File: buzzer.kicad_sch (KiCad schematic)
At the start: 0 parts

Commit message: Buzzer sheet 1st draft finished
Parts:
- added J1: Conn_01x02, symbol Connector_Generic:Conn_01x02
- added R5, R6: R, symbol Hestres_Standard_Lib:R
- added U4: UCC23313DWYR, SOIC6_DWY_TEX, symbol ProjGateDriver:UCC23313DWYR
- added U5: RD3L01BATTL1, DPAK_1BATTL1_ROM, symbol ProjPMOS:RD3L01BATTL1
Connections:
- new net: R6.1, U4.5 (VOUT)
- new net: J1.1 (Pin_1), R5.1, U5.2 (Drain)
- new net: R6.2, U5.1 (Gate)
- new net 18V: U4.6 (VCC), U5.3 (Source)
- new net GND: J1.2 (Pin_2), R5.2, U4.3 (CATHODE), U4.4 (VEE)
- new net PWM: U4.1 (ANODE)
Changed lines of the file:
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@@
 (kicad_sch (version 20230121) (generator eeschema)
   (paper "A4")
+  (junction (at 181.61 87.63) (diameter 0) (color 0 0 0 0)
+  )
+  (junction (at 69.85 132.715) (diameter 0) (color 0 0 0 0)
+  )
+  (junction (at 115.57 132.715) (diameter 0) (color 0 0 0 0)
+  )
+  (junction (at 182.88 125.095) (diameter 0) (color 0 0 0 0)
+  )
+  (junction (at 182.88 132.715) (diameter 0) (color 0 0 0 0)
+  )
+  (wire (pts (xy 193.675 125.095) (xy 182.88 125.095))
+    (stroke (width 0) (type default))
+  )
+  (wire (pts (xy 182.88 109.855) (xy 182.88 125.095))
+    (stroke (width 0) (type default))
+  )
+  (wire (pts (xy 115.57 107.315) (xy 121.92 107.315))
+    (stroke (width 0) (type default))
+  )
+  (wire (pts (xy 193.675 132.715) (xy 182.88 132.715))
+    (stroke (width 0) (type default))
+  )
+  (wire (pts (xy 69.85 132.715) (xy 115.57 132.715))
+    (stroke (width 0) (type default))
+  )
+  (wire (pts (xy 115.57 132.715) (xy 182.88 132.715))
+    (stroke (width 0) (type default))
+  )
+  (wire (pts (xy 180.975 109.855) (xy 182.88 109.855))
+    (stroke (width 0) (type default))
+  )
+  (wire (pts (xy 129.54 107.315) (xy 135.255 107.315))
+    (stroke (width 0) (type default))
+  )
+  (wire (pts (xy 115.57 87.63) (xy 181.61 87.63))
+    (stroke (width 0) (type default))
+  )
+  (wire (pts (xy 67.31 132.715) (xy 69.85 132.715))
+    (stroke (width 0) (type default))
+  )
+  (wire (pts (xy 193.675 130.175) (xy 193.675 132.715))
+    (stroke (width 0) (type default))
+  )
+  (wire (pts (xy 193.675 127.635) (xy 193.675 125.095))
+    (stroke (width 0) (type default))
+  )
+  (wire (pts (xy 67.31 104.775) (xy 69.85 104.775))
+    (stroke (width 0) (type default))
+  )
+  (wire (pts (xy 115.57 109.855) (xy 115.57 132.715))
+    (stroke (width 0) (type default))
+  )
+  (wire (pts (xy 69.85 109.855) (xy 69.85 132.715))
+    (stroke (width 0) (type default))
+  )
+  (wire (pts (xy 180.975 107.315) (xy 181.61 107.315))
+    (stroke (width 0) (type default))
+  )
+  (wire (pts (xy 181.61 107.315) (xy 181.61 87.63))
+    (stroke (width 0) (type default))
+  )
+  (wire (pts (xy 115.57 87.63) (xy 115.57 104.775))
+    (stroke (width 0) (type default))
+  )
+  (wire (pts (xy 181.61 87.63) (xy 183.515 87.63))
+    (stroke (width 0) (type default))
+  )
+  (hierarchical_label "GND" (shape input) (at 67.31 132.715 180) (fields_autoplaced)
+    (effects (font (size 1.27 1.27)) (justify right))
+  )
+  (hierarchical_label "PWM" (shape input) (at 67.31 104.775 180) (fields_autoplaced)
+    (effects (font (size 1.27 1.27)) (justify right))
+  )
+  (hierarchical_label "18V" (shape input) (at 183.515 87.63 0) (fields_autoplaced)
+    (effects (font (size 1.27 1.27)) (justify left))
+  )
+  (symbol (lib_id "ProjGateDriver:UCC23313DWYR") (at 69.85 104.775 0) (unit 1)
+    (in_bom yes) (on_board yes) (dnp no) (fields_autoplaced)
+    (property "Reference" "U4" (at 92.71 94.615 0)
+      (effects (font (size 1.524 1.524)))
+    )
+    (property "Value" "UCC23313DWYR" (at 92.71 97.155 0)
+      (effects (font (size 1.524 1.524)))
+    )
+    (property "Footprint" "SOIC6_DWY_TEX" (at 69.85 104.775 0)
+      (effects (font (size 1.27 1.27) italic) hide)
+    )
+    (property "Datasheet" "UCC23313DWYR" (at 69.85 104.775 0)
+      (effects (font (size 1.27 1.27) italic) hide)
+    )
+    (pin "1")
+    (pin "2")
+    (pin "3")
+    (pin "4")
+    (pin "5")
+    (pin "6")
+    (instances
+      (project "CatLasers"
+        (path "/b94f5b10-ee0c-4425-b025-e3a8bb3cc7b0/d2efd2c4-3cc3-446b-9153-cc0ad0bf95db"
+          (reference "U4") (unit 1)
+        )
+      )
+    )
+  )
+  (symbol (lib_id "Hestres_Standard_Lib:R") (at 182.88 128.905 0) (unit 1)
+    (in_bom yes) (on_board yes) (dnp no) (fields_autoplaced)
+    (property "Reference" "R5" (at 184.785 127.635 0)
+      (effects (font (size 1.27 1.27)) (justify left))
+    )
+    (property "Value" "R" (at 184.785 130.175 0)
+      (effects (font (size 1.27 1.27)) (justify left))
+    )
+    (property "Footprint" "" (at 181.102 128.905 90)
+      (effects (font (size 1.27 1.27)) hide)
+    )
+    (property "Datasheet" "~" (at 182.88 128.905 0)
+      (effects (font (size 1.27 1.27)) hide)
+    )
+    (pin "1")
+    (pin "2")
+    (instances
+      (project "CatLasers"
+        (path "/b94f5b10-ee0c-4425-b025-e3a8bb3cc7b0/d2efd2c4-3cc3-446b-9153-cc0ad0bf95db"
+          (reference "R5") (unit 1)
+        )
+      )
+    )
+  )
+  (symbol (lib_id "Connector_Generic:Conn_01x02") (at 198.755 127.635 0) (unit 1)
+    (in_bom yes) (on_board yes) (dnp no) (fields_autoplaced)
+    (property "Reference" "J1" (at 201.93 127.635 0)
+      (effects (font (size 1.27 1.27)) (justify left))
+    )
+    (property "Value" "Conn_01x02" (at 201.93 130.175 0)
+      (effects (font (size 1.27 1.27)) (justify left))
+    )
+    (property "Footprint" "" (at 198.755 127.635 0)
+      (effects (font (size 1.27 1.27)) hide)
+    )
+    (property "Datasheet" "~" (at 198.755 127.635 0)
+      (effects (font (size 1.27 1.27)) hide)
+    )
+    (pin "1")
+    (pin "2")
+    (instances
+      (project "CatLasers"
+        (path "/b94f5b10-ee0c-4425-b025-e3a8bb3cc7b0/d2efd2c4-3cc3-446b-9153-cc0ad0bf95db"
+          (reference "J1") (unit 1)
+        )
+      )
+    )
+  )
+  (symbol (lib_id "ProjPMOS:RD3L01BATTL1") (at 135.255 107.315 0) (unit 1)
+    (in_bom yes) (on_board yes) (dnp no) (fields_autoplaced)
+    (property "Reference" "U5" (at 158.115 97.155 0)
+      (effects (font (size 1.524 1.524)))
+    )
+    (property "Value" "RD3L01BATTL1" (at 158.115 99.695 0)
+      (effects (font (size 1.524 1.524)))
+    )
+    (property "Footprint" "DPAK_1BATTL1_ROM" (at 135.255 107.315 0)
+      (effects (font (size 1.27 1.27) italic) hide)
+    )
+    (property "Datasheet" "RD3L01BATTL1" (at 135.255 107.315 0)
+      (effects (font (size 1.27 1.27) italic) hide)
+    )
+    (pin "1")
+    (pin "2")
+    (pin "3")
+    (instances
+      (project "CatLasers"
+        (path "/b94f5b10-ee0c-4425-b025-e3a8bb3cc7b0/d2efd2c4-3cc3-446b-9153-cc0ad0bf95db"
+          (reference "U5") (unit 1)
+        )
+      )
+    )
+  )
+  (symbol (lib_id "Hestres_Standard_Lib:R") (at 125.73 107.315 90) (unit 1)
+    (in_bom yes) (on_board yes) (dnp no) (fields_autoplaced)
+    (property "Reference" "R6" (at 125.73 101.6 90)
+      (effects (font (size 1.27 1.27)))
+    )
+    (property "Value" "R" (at 125.73 104.14 90)
+      (effects (font (size 1.27 1.27)))
+    )
+    (property "Footprint" "" (at 125.73 109.093 90)
+      (effects (font (size 1.27 1.27)) hide)
+    )
+    (property "Datasheet" "~" (at 125.73 107.315 0)
+      (effects (font (size 1.27 1.27)) hide)
+    )
+    (pin "1")
+    (pin "2")
+    (instances
+      (project "CatLasers"
+        (path "/b94f5b10-ee0c-4425-b025-e3a8bb3cc7b0/d2efd2c4-3cc3-446b-9153-cc0ad0bf95db"
+          (reference "R6") (unit 1)
+        )
+      )
+    )
+  )
 )

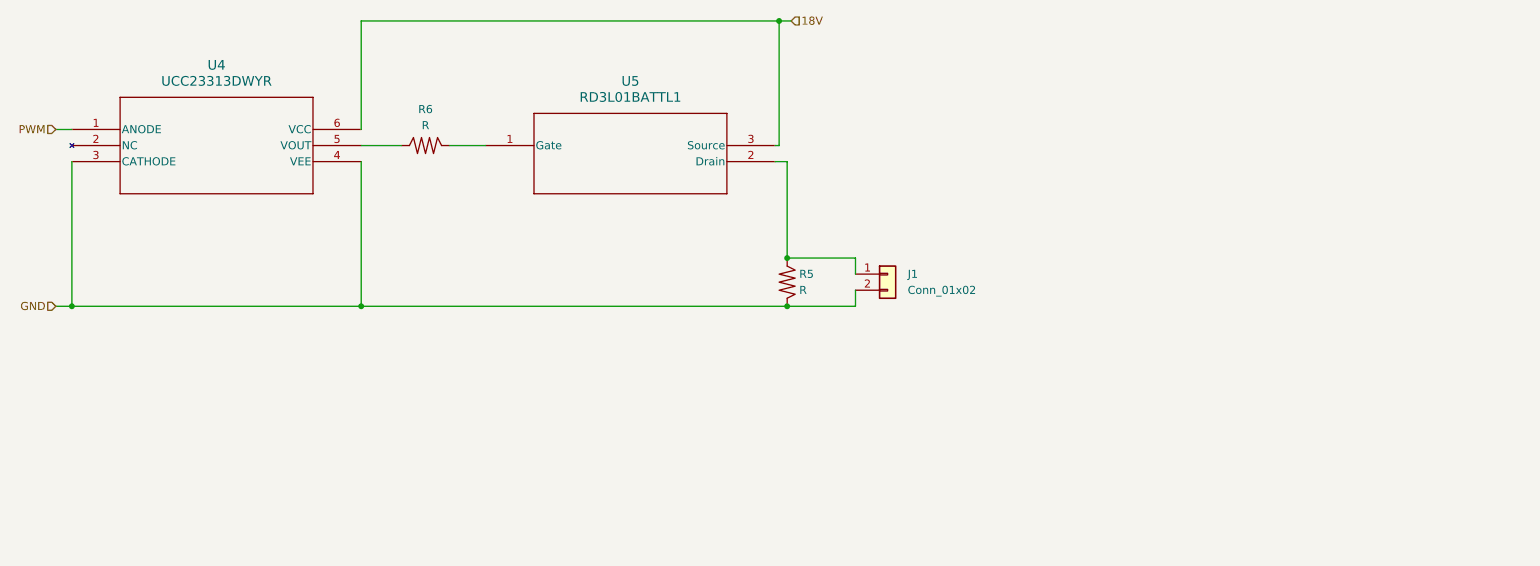
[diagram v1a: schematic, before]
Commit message: Gate Driver resistor chosen and footprint added
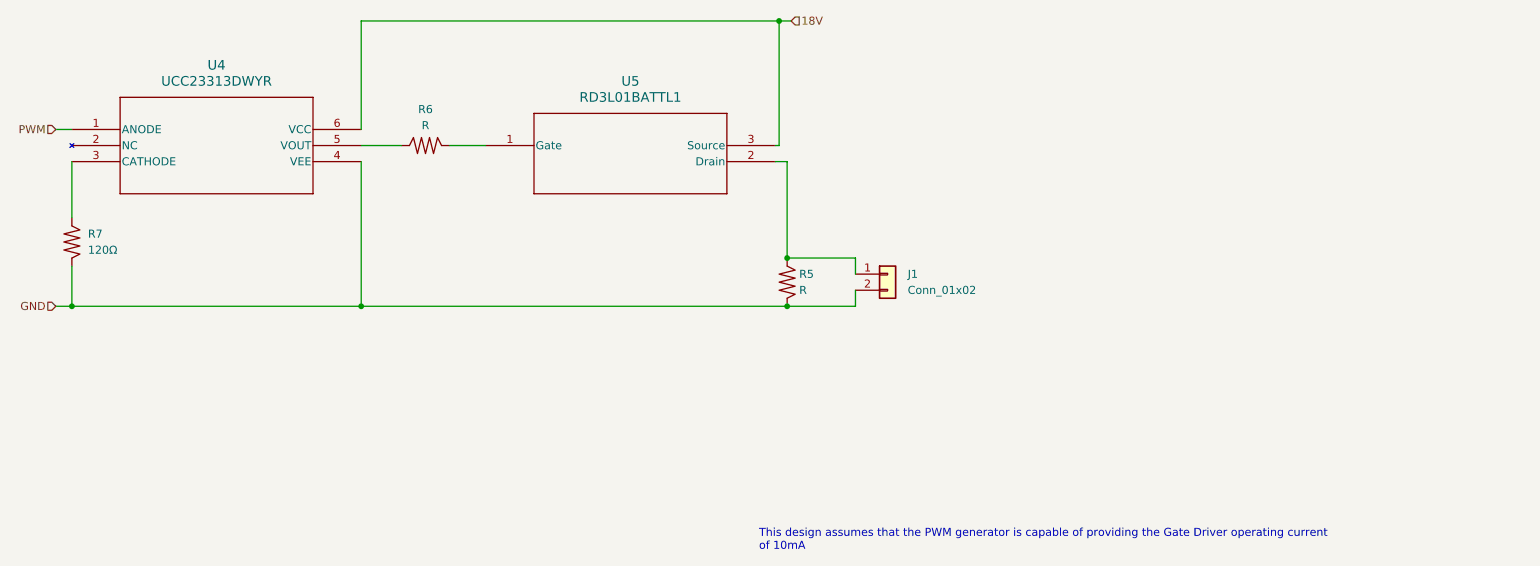
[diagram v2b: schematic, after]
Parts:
- added R7: 120Ω, Resistor_SMD:R_0805_2012Metric, symbol Hestres_Standard_Lib:R
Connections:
- net GND: now also R7.2; no longer U4.3 (CATHODE)
- new net: R7.1, U4.3 (CATHODE)
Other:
- note added: "This design assumes that the PWM generator is capable of providing the Gate Driver operating current of 10mA"
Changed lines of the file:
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@@
+    (stroke (width 0) (type default))
+  )
+  (wire (pts (xy 69.85 126.365) (xy 69.85 132.715))
     (stroke (width 0) (type default))
   )
@@
     (stroke (width 0) (type default))
   )
-  (wire (pts (xy 69.85 109.855) (xy 69.85 132.715))
+  (wire (pts (xy 69.85 109.855) (xy 69.85 118.745))
     (stroke (width 0) (type default))
   )
@@
   (wire (pts (xy 181.61 87.63) (xy 183.515 87.63))
     (stroke (width 0) (type default))
+  )
+  (text "This design assumes that the PWM generator is capable of providing the Gate Driver operating current \nof 10mA"
+    (at 178.435 171.45 0)
+    (effects (font (size 1.27 1.27)) (justify left bottom))
   )
   (hierarchical_label "GND" (shape input) (at 67.31 132.715 180) (fields_autoplaced)
@@
         )
       )
+    )
+  )
+  (symbol (lib_id "Hestres_Standard_Lib:R") (at 69.85 122.555 0) (unit 1)
+    (in_bom yes) (on_board yes) (dnp no) (fields_autoplaced)
+    (property "Reference" "R7" (at 72.39 121.285 0)
+      (effects (font (size 1.27 1.27)) (justify left))
+    )
+    (property "Value" "120Ω" (at 72.39 123.825 0)
+      (effects (font (size 1.27 1.27)) (justify left))
+    )
+    (property "Footprint" "Resistor_SMD:R_0805_2012Metric" (at 68.072 122.555 90)
+      (effects (font (size 1.27 1.27)) hide)
+    )
+    (property "Datasheet" "~" (at 69.85 122.555 0)
+      (effects (font (size 1.27 1.27)) hide)
+    )
+    (pin "1")
+    (pin "2")
+    (instances
+      (project "CatLasers"
+        (path "/b94f5b10-ee0c-4425-b025-e3a8bb3cc7b0/d2efd2c4-3cc3-446b-9153-cc0ad0bf95db"
+          (reference "R7") (unit 1)
+        )
+      )

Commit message: Some cleanup
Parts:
- U4: footprint SOIC6_DWY_TEX -> (none)
- U5: footprint DPAK_1BATTL1_ROM -> (none)
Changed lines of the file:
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@@
       (effects (font (size 1.524 1.524)))
     )
-    (property "Footprint" "SOIC6_DWY_TEX" (at 69.85 104.775 0)
+    (property "Footprint" "" (at 69.85 104.775 0)
       (effects (font (size 1.27 1.27) italic) hide)
     )
@@
       (effects (font (size 1.524 1.524)))
     )
-    (property "Footprint" "DPAK_1BATTL1_ROM" (at 135.255 107.315 0)
+    (property "Footprint" "" (at 135.255 107.315 0)
       (effects (font (size 1.27 1.27) italic) hide)
     )

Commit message: Remaining Footprints Assigned
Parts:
- J1: footprint (none) -> Connector_PinHeader_2.54mm:PinHeader_1x02_P2.54mm_Vertical
- R5, R6: footprint (none) -> Resistor_SMD:R_0805_2012Metric
- U4: footprint (none) -> Proj:SOD-123FL_MCC
- U5: footprint (none) -> Proj:RD3L01BATTL1_ROM
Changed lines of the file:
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@@
       (effects (font (size 1.524 1.524)))
     )
-    (property "Footprint" "" (at 69.85 104.775 0)
+    (property "Footprint" "Proj:SOD-123FL_MCC" (at 69.85 104.775 0)
       (effects (font (size 1.27 1.27) italic) hide)
     )
@@
       (effects (font (size 1.27 1.27)) (justify left))
     )
-    (property "Footprint" "" (at 181.102 128.905 90)
+    (property "Footprint" "Resistor_SMD:R_0805_2012Metric" (at 181.102 128.905 90)
       (effects (font (size 1.27 1.27)) hide)
     )
@@
       (effects (font (size 1.27 1.27)) (justify left))
     )
-    (property "Footprint" "" (at 198.755 127.635 0)
+    (property "Footprint" "Connector_PinHeader_2.54mm:PinHeader_1x02_P2.54mm_Vertical" (at 198.755 127.635 0)
       (effects (font (size 1.27 1.27)) hide)
     )
@@
       (effects (font (size 1.524 1.524)))
     )
-    (property "Footprint" "" (at 135.255 107.315 0)
+    (property "Footprint" "Proj:RD3L01BATTL1_ROM" (at 135.255 107.315 0)
       (effects (font (size 1.27 1.27) italic) hide)
     )
@@
       (effects (font (size 1.27 1.27)))
     )
-    (property "Footprint" "" (at 125.73 109.093 90)
+    (property "Footprint" "Resistor_SMD:R_0805_2012Metric" (at 125.73 109.093 90)
       (effects (font (size 1.27 1.27)) hide)
     )

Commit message: Annotations
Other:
- note added: "R5 is left undefined to allow for testing. To reduce power consumption, the highest resistance - without restricting the full oscillations of the piezzo - should be selected"
- note added: "R6 is left undefined to be decided later."
- note added: "This connector is for the speaker. Currently, the piezzo leads will be soldered directly to the board."
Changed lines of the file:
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@@
     (stroke (width 0) (type default))
+  )
+  (text "R5 is left undefined to allow\nfor testing. To reduce power\nconsumption, the highest\nresistance - without restricting\nthe full oscillations of the\npiezzo - should be selected"
+    (at 168.275 147.955 0)
+    (effects (font (size 1.27 1.27)) (justify left bottom))
   )
   (text "This design assumes that the PWM generator is capable of providing the Gate Driver operating current \nof 10mA"
@@
     (effects (font (size 1.27 1.27)) (justify left bottom))
   )
+  (text "This connector is for the speaker. Currently, the piezzo leads\nwill be soldered directly to the board."
+    (at 196.85 123.825 0)
+    (effects (font (size 1.27 1.27)) (justify left bottom))
+  )
+  (text "R6 is left undefined to be\ndecided later." (at 116.84 114.3 0)
+    (effects (font (size 1.27 1.27)) (justify left bottom))
+  )

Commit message: Components on PCB, all warnings and error fixed
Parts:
- U4: footprint Proj:SOD-123FL_MCC -> Proj:SOIC6_DWY_TEX
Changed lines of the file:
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@@
       (effects (font (size 1.524 1.524)))
     )
-    (property "Footprint" "Proj:SOD-123FL_MCC" (at 69.85 104.775 0)
+    (property "Footprint" "Proj:SOIC6_DWY_TEX" (at 69.85 104.775 0)
       (effects (font (size 1.27 1.27) italic) hide)
     )

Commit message: Piezzo Layout
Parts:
- J1: value Conn_01x02 -> Piezzo
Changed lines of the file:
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@@
       (effects (font (size 1.27 1.27)) (justify left))
     )
-    (property "Value" "Conn_01x02" (at 201.93 130.175 0)
+    (property "Value" "Piezzo" (at 201.93 130.175 0)
       (effects (font (size 1.27 1.27)) (justify left))
     )

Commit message: DRC Pass
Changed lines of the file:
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@@
     )
   )
-  (symbol (lib_id "Hestres_Standard_Lib:R") (at 69.85 122.555 0) (unit 1)
-    (in_bom yes) (on_board yes) (dnp no) (fields_autoplaced)
-    (property "Reference" "R7" (at 72.39 121.285 0)
+  (symbol (lib_id "Hestres_Standard_Lib:R") (at 69.85 122.555 0) (mirror y) (unit 1)
+    (in_bom yes) (on_board yes) (dnp no)
+    (property "Reference" "R7" (at 67.31 121.285 0)
       (effects (font (size 1.27 1.27)) (justify left))
     )
-    (property "Value" "120Ω" (at 72.39 123.825 0)
+    (property "Value" "120Ω" (at 67.31 123.825 0)
       (effects (font (size 1.27 1.27)) (justify left))
     )
-    (property "Footprint" "Resistor_SMD:R_0805_2012Metric" (at 68.072 122.555 90)
+    (property "Footprint" "Resistor_SMD:R_0805_2012Metric" (at 71.628 122.555 90)
       (effects (font (size 1.27 1.27)) hide)
     )
